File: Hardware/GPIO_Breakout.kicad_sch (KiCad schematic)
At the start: 2 parts, among them J8 GPIO Breakout

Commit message: Overall Routing Complete!!!
Version2
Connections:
- net GPIO13: now also D6.7 (K/A_6), J8.4 (Pin_4); no longer D6.3 (K/A_2), J8.3 (Pin_3)
- net GPIO14: now also D6.6 (K/A_5), J8.6 (Pin_6); no longer D6.4 (K/A_3), J8.4 (Pin_4)
- net GPIO15: now also J8.8 (Pin_8); no longer J8.6 (Pin_6)
- net GPIO4: now also J8.7 (Pin_7); no longer J8.2 (Pin_2)
- removed net GPIO16: D6.6 (K/A_5), J8.7 (Pin_7)
- removed net GPIO39: D6.7 (K/A_6), J8.8 (Pin_8)
- new net GPIO1: D6.4 (K/A_3), J8.2 (Pin_2)
- new net GPIO2: D6.3 (K/A_2), J8.3 (Pin_3)
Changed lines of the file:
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@@
 		)
 	)
-	(hierarchical_label "GPIO39"
+	(hierarchical_label "GPIO13"
 		(shape bidirectional)
 		(at 82.55 52.07 0)
@@
 		)
 	)
-	(hierarchical_label "GPIO16"
+	(hierarchical_label "GPIO4"
 		(shape bidirectional)
 		(at 114.3 54.61 180)
@@
 		)
 	)
-	(hierarchical_label "GPIO13"
+	(hierarchical_label "GPIO2"
 		(shape bidirectional)
 		(at 52.07 52.07 180)
@@
 		)
 	)
-	(hierarchical_label "GPIO14"
+	(hierarchical_label "GPIO1"
 		(shape bidirectional)
 		(at 52.07 54.61 180)
@@
 		)
 	)
-	(hierarchical_label "GPIO4"
+	(hierarchical_label "GPIO1"
 		(shape bidirectional)
 		(at 114.3 41.91 180)
@@
 		)
 	)
-	(hierarchical_label "GPIO39"
+	(hierarchical_label "GPIO15"
 		(shape bidirectional)
 		(at 114.3 57.15 180)
@@
 		)
 	)
-	(hierarchical_label "GPIO16"
+	(hierarchical_label "GPIO14"
 		(shape bidirectional)
 		(at 82.55 49.53 0)
@@
 		)
 	)
-	(hierarchical_label "GPIO13"
+	(hierarchical_label "GPIO2"
 		(shape bidirectional)
 		(at 114.3 44.45 180)
@@
 		)
 	)
-	(hierarchical_label "GPIO14"
+	(hierarchical_label "GPIO13"
 		(shape bidirectional)
 		(at 114.3 46.99 180)
@@
 		)
 	)
-	(hierarchical_label "GPIO15"
+	(hierarchical_label "GPIO14"
 		(shape bidirectional)
 		(at 114.3 52.07 180)

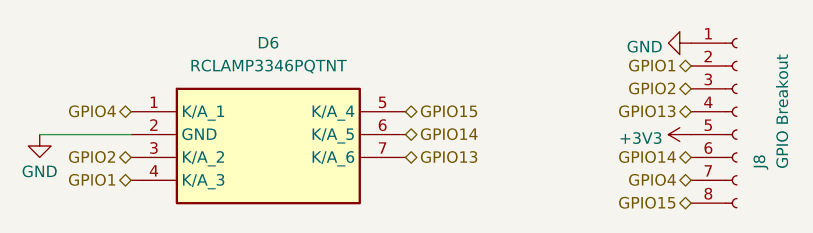
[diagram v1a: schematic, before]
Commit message: Routing Improvement
Version 3. Mainly solved 3 problem: 1. clock and decoupler closer to microcontroller; 2. Route of Data+ and Data- neater; 3. wider trace for 6v and 16.8v
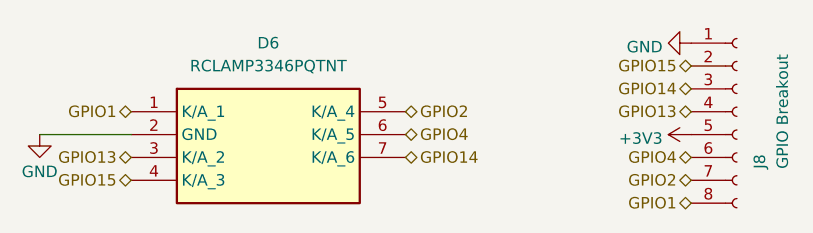
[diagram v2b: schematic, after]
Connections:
- net GPIO1: now also D6.1 (K/A_1), J8.8 (Pin_8); no longer D6.4 (K/A_3), J8.2 (Pin_2)
- net GPIO13: now also D6.3 (K/A_2); no longer D6.7 (K/A_6)
- net GPIO14: now also D6.7 (K/A_6), J8.3 (Pin_3); no longer D6.6 (K/A_5), J8.6 (Pin_6)
- net GPIO15: now also D6.4 (K/A_3), J8.2 (Pin_2); no longer D6.5 (K/A_4), J8.8 (Pin_8)
- net GPIO2: now also D6.5 (K/A_4), J8.7 (Pin_7); no longer D6.3 (K/A_2), J8.3 (Pin_3)
- net GPIO4: now also D6.6 (K/A_5), J8.6 (Pin_6); no longer D6.1 (K/A_1), J8.7 (Pin_7)
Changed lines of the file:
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@@
 		)
 	)
-	(hierarchical_label "GPIO13"
+	(hierarchical_label "GPIO14"
 		(shape bidirectional)
 		(at 82.55 52.07 0)
@@
 		)
 	)
-	(hierarchical_label "GPIO4"
+	(hierarchical_label "GPIO2"
 		(shape bidirectional)
 		(at 114.3 54.61 180)
@@
 		)
 	)
-	(hierarchical_label "GPIO2"
+	(hierarchical_label "GPIO13"
 		(shape bidirectional)
 		(at 52.07 52.07 180)
@@
 		)
 	)
-	(hierarchical_label "GPIO1"
+	(hierarchical_label "GPIO15"
 		(shape bidirectional)
 		(at 52.07 54.61 180)
@@
 		)
 	)
-	(hierarchical_label "GPIO1"
+	(hierarchical_label "GPIO15"
 		(shape bidirectional)
 		(at 114.3 41.91 180)
@@
 		)
 	)
-	(hierarchical_label "GPIO15"
+	(hierarchical_label "GPIO1"
 		(shape bidirectional)
 		(at 114.3 57.15 180)
@@
 		)
 	)
-	(hierarchical_label "GPIO14"
+	(hierarchical_label "GPIO4"
 		(shape bidirectional)
 		(at 82.55 49.53 0)
@@
 		)
 	)
-	(hierarchical_label "GPIO2"
+	(hierarchical_label "GPIO14"
 		(shape bidirectional)
 		(at 114.3 44.45 180)
@@
 		)
 	)
-	(hierarchical_label "GPIO4"
+	(hierarchical_label "GPIO1"
 		(shape bidirectional)
 		(at 52.07 46.99 180)
@@
 		)
 	)
-	(hierarchical_label "GPIO15"
+	(hierarchical_label "GPIO2"
 		(shape bidirectional)
 		(at 82.55 46.99 0)
@@
 		)
 	)
-	(hierarchical_label "GPIO14"
+	(hierarchical_label "GPIO4"
 		(shape bidirectional)
 		(at 114.3 52.07 180)

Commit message: Filled zones and via location
Version 4. allocate filled zones and vias, also reassigned pins from microcontroller
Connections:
- net GPIO1 renamed TVS1
- net GPIO13 renamed TVS3
- net GPIO14 renamed TVS7
- net GPIO15 renamed TVS4
- net GPIO2 renamed TVS5
- net GPIO4 renamed TVS6
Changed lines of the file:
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@@
 		)
 	)
-	(hierarchical_label "GPIO14"
+	(hierarchical_label "TVS7"
 		(shape bidirectional)
 		(at 82.55 52.07 0)
@@
 		)
 	)
-	(hierarchical_label "GPIO2"
+	(hierarchical_label "TVS5"
 		(shape bidirectional)
 		(at 114.3 54.61 180)
@@
 		)
 	)
-	(hierarchical_label "GPIO13"
+	(hierarchical_label "TVS3"
 		(shape bidirectional)
 		(at 52.07 52.07 180)
@@
 		)
 	)
-	(hierarchical_label "GPIO15"
+	(hierarchical_label "TVS4"
 		(shape bidirectional)
 		(at 52.07 54.61 180)
@@
 		)
 	)
-	(hierarchical_label "GPIO15"
+	(hierarchical_label "TVS4"
 		(shape bidirectional)
 		(at 114.3 41.91 180)
@@
 		)
 	)
-	(hierarchical_label "GPIO1"
+	(hierarchical_label "TVS1"
 		(shape bidirectional)
 		(at 114.3 57.15 180)
@@
 		)
 	)
-	(hierarchical_label "GPIO4"
+	(hierarchical_label "TVS6"
 		(shape bidirectional)
 		(at 82.55 49.53 0)
@@
 		)
 	)
-	(hierarchical_label "GPIO14"
+	(hierarchical_label "TVS7"
 		(shape bidirectional)
 		(at 114.3 44.45 180)
@@
 		)
 	)
-	(hierarchical_label "GPIO13"
+	(hierarchical_label "TVS3"
 		(shape bidirectional)
 		(at 114.3 46.99 180)
@@
 		)
 	)
-	(hierarchical_label "GPIO1"
+	(hierarchical_label "TVS1"
 		(shape bidirectional)
 		(at 52.07 46.99 180)
@@
 		)
 	)
-	(hierarchical_label "GPIO2"
+	(hierarchical_label "TVS5"
 		(shape bidirectional)
 		(at 82.55 46.99 0)
@@
 		)
 	)
-	(hierarchical_label "GPIO4"
+	(hierarchical_label "TVS6"
 		(shape bidirectional)
 		(at 114.3 52.07 180)
